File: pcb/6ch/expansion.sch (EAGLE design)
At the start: 48 parts, among them IC3 STM32F042F4, J7 AUDIO_JACK_3.5MM_PTH, J8 AUDIO_JACK_3.5MM_PTH, SW3 324_SW, SW4 324_SW, U1 USBC_16P, U2 USBC_16P, U4 XC6206_DEV

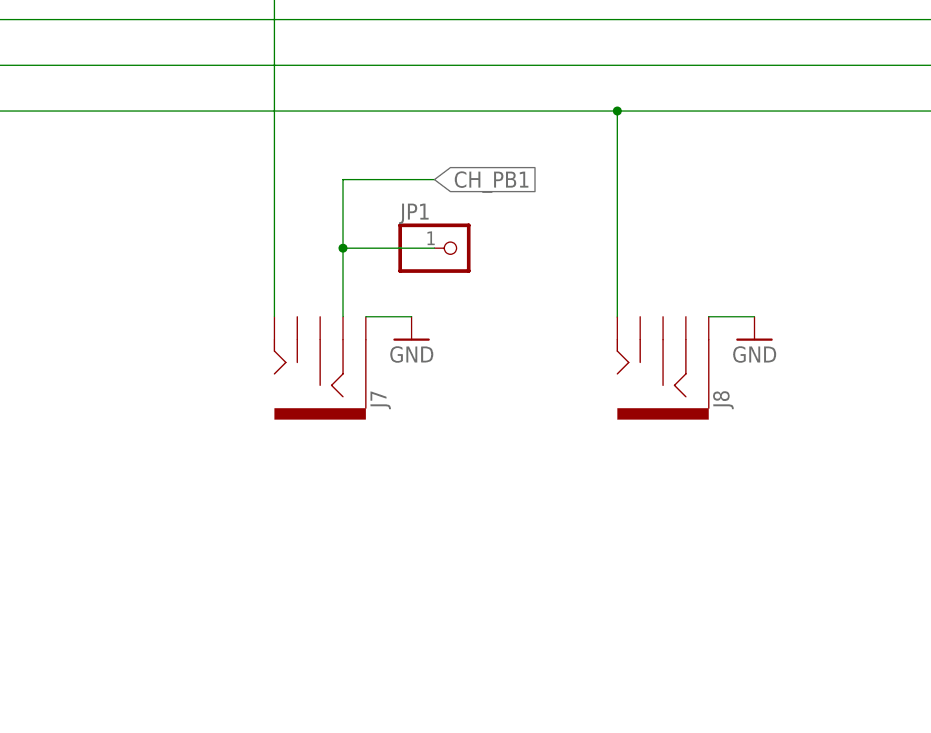
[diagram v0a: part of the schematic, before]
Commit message: added PB1 LED
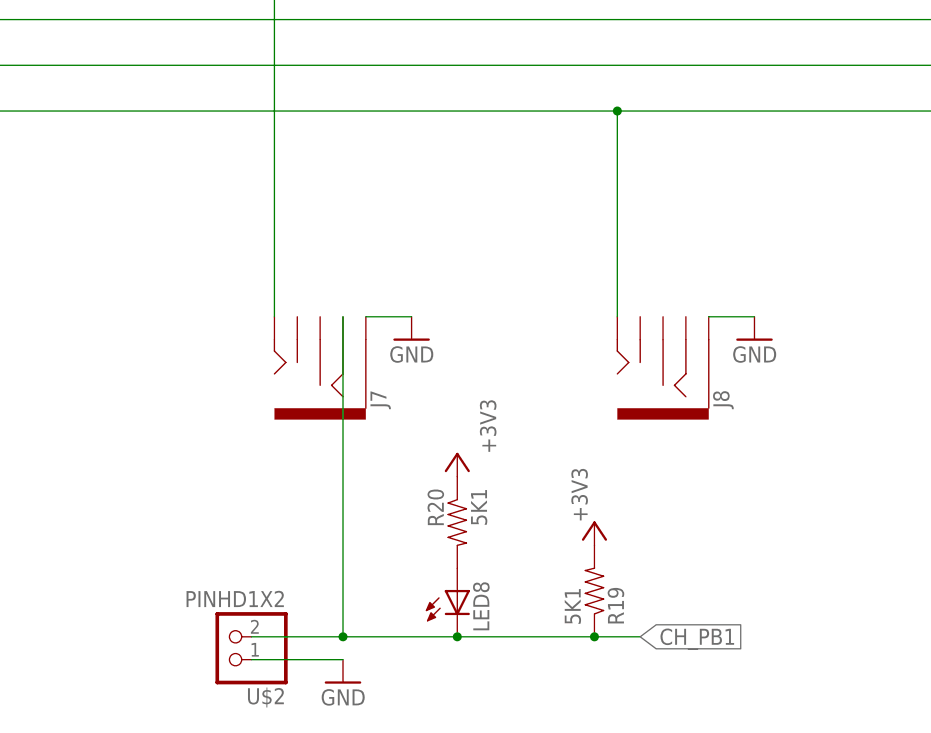
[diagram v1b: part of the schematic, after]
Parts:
- removed JP1: (no value), adafruit_changed:PINHD-1X1CB
- added LED8: (no value), adafruit:LEDCHIP-LED0805
- added R19, R20: 5K1, joyAnalog:RESISTOR0805-RES
- added U$2: PINHD1X2, adafruit_changed:PINHD1X2
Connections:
- new net N$9: LED8.A, R20.2
- net +3V3: now also R19.2, R20.1
- net CH_PB1: now also LED8.C, R19.1, U$2.2; no longer JP1.1
- net GND: now also U$2.1
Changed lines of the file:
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@@
 <part name="GND15" library="supply1" deviceset="GND" device=""/>
 <part name="GND17" library="supply1" deviceset="GND" device=""/>
-<part name="JP1" library="adafruit_changed" deviceset="PINHD-1X1" device="CB"/>
 <part name="JP2" library="pinhead" library_urn="urn:adsk.eagle:library:325" deviceset="PINHD-2X3" device="" package3d_urn="urn:adsk.eagle:package:22462/2"/>
 <part name="GND19" library="supply1" deviceset="GND" device=""/>
@@
 <part name="U$1" library="adafruit_changed" deviceset="PINHD1X2" device=""/>
 <part name="U$3" library="adafruit_changed" deviceset="PINHD1X2" device=""/>
+<part name="R19" library="joyAnalog" deviceset="RESISTOR" device="0805-RES" value="5K1"/>
+<part name="+3V20" library="supply1" library_urn="urn:adsk.eagle:library:371" deviceset="+3V3" device=""/>
+<part name="LED8" library="adafruit" deviceset="LED" device="CHIP-LED0805"/>
+<part name="R20" library="joyAnalog" deviceset="RESISTOR" device="0805-RES" value="5K1"/>
+<part name="+3V21" library="supply1" library_urn="urn:adsk.eagle:library:371" deviceset="+3V3" device=""/>
+<part name="U$2" library="adafruit_changed" deviceset="PINHD1X2" device=""/>
+<part name="GND21" library="supply1" deviceset="GND" device=""/>
 </parts>
 <sheets>
@@
 <attribute name="VALUE" x="-86.36" y="-111.76" size="1.778" layer="96" rot="MR0"/>
 </instance>
-<instance part="JP1" gate="G$1" x="-121.92" y="-99.06" smashed="yes">
-<attribute name="NAME" x="-128.27" y="-95.885" size="1.778" layer="95"/>
-<attribute name="VALUE" x="-128.27" y="-104.14" size="1.778" layer="96"/>
-</instance>
 <instance part="JP2" gate="A" x="149.86" y="-43.18" smashed="yes">
 <attribute name="NAME" x="143.51" y="-37.465" size="1.778" layer="95"/>
@@
 <attribute name="NAME" x="-34.29" y="-27.305" size="1.778" layer="95"/>
 <attribute name="VALUE" x="-34.29" y="-38.1" size="1.778" layer="96"/>
+</instance>
+<instance part="R19" gate="G$1" x="-106.68" y="-137.16" smashed="yes" rot="MR90">
+<attribute name="NAME" x="-105.1814" y="-140.97" size="1.778" layer="95" rot="MR90"/>
+<attribute name="VALUE" x="-109.982" y="-140.97" size="1.778" layer="96" rot="MR90"/>
+<attribute name="NAME" x="-105.1814" y="-140.97" size="1.778" layer="95" rot="MR90"/>
+<attribute name="VALUE" x="-109.982" y="-140.97" size="1.778" layer="96" rot="MR90"/>
+</instance>
+<instance part="+3V20" gate="G$1" x="-106.68" y="-129.54" smashed="yes" rot="MR0">
+<attribute name="VALUE" x="-109.22" y="-129.54" size="1.778" layer="96" rot="MR90"/>
+</instance>
+<instance part="LED8" gate="G$1" x="-121.92" y="-137.16" smashed="yes">
+<attribute name="NAME" x="-118.364" y="-141.732" size="1.778" layer="95" rot="R90"/>
+<attribute name="VALUE" x="-116.205" y="-141.732" size="1.778" layer="96" rot="R90"/>
+</instance>
+<instance part="R20" gate="G$1" x="-121.92" y="-129.54" smashed="yes" rot="MR270">
+<attribute name="NAME" x="-123.4186" y="-125.73" size="1.778" layer="95" rot="MR270"/>
+<attribute name="VALUE" x="-118.618" y="-125.73" size="1.778" layer="96" rot="MR270"/>
+<attribute name="NAME" x="-123.4186" y="-125.73" size="1.778" layer="95" rot="MR270"/>
+<attribute name="VALUE" x="-118.618" y="-125.73" size="1.778" layer="96" rot="MR270"/>
+</instance>
+<instance part="+3V21" gate="G$1" x="-121.92" y="-121.92" smashed="yes" rot="MR0">
+<attribute name="VALUE" x="-119.38" y="-121.92" size="1.778" layer="96" rot="MR90"/>
+</instance>
+<instance part="U$2" gate="1" x="-147.32" y="-142.24" smashed="yes" rot="R180">
+<attribute name="NAME" x="-140.97" y="-147.955" size="1.778" layer="95" rot="R180"/>
+<attribute name="VALUE" x="-140.97" y="-137.16" size="1.778" layer="96" rot="R180"/>
+</instance>
+<instance part="GND21" gate="1" x="-134.62" y="-147.32" smashed="yes" rot="MR0">
+<attribute name="VALUE" x="-132.08" y="-149.86" size="1.778" layer="96" rot="MR0"/>
 </instance>
 </instances>
@@
 <junction x="147.32" y="-43.18"/>
 </segment>
+<segment>
+<pinref part="U$2" gate="1" pin="1"/>
+<pinref part="GND21" gate="1" pin="GND"/>
+<wire x1="-144.78" y1="-144.78" x2="-134.62" y2="-144.78" width="0.1524" layer="91"/>
+</segment>
 </net>
 <net name="+3V3" class="0">
@@
 <wire x1="154.94" y1="-45.72" x2="147.32" y2="-45.72" width="0.1524" layer="91"/>
 <junction x="154.94" y="-45.72"/>
+</segment>
+<segment>
+<pinref part="R19" gate="G$1" pin="2"/>
+<pinref part="+3V20" gate="G$1" pin="+3V3"/>
+</segment>
+<segment>
+<pinref part="R20" gate="G$1" pin="1"/>
+<pinref part="+3V21" gate="G$1" pin="+3V3"/>
 </segment>
 </net>
@@
 </segment>
 <segment>
-<wire x1="-124.46" y1="-91.44" x2="-134.62" y2="-91.44" width="0.1524" layer="91"/>
-<label x="-124.46" y="-91.44" size="1.778" layer="95" xref="yes"/>
+<wire x1="-101.6" y1="-142.24" x2="-106.68" y2="-142.24" width="0.1524" layer="91"/>
+<label x="-101.6" y="-142.24" size="1.778" layer="95" xref="yes"/>
 <pinref part="J7" gate="G$1" pin="RING"/>
-<wire x1="-134.62" y1="-106.68" x2="-134.62" y2="-99.06" width="0.1524" layer="91"/>
-<pinref part="JP1" gate="G$1" pin="1"/>
-<wire x1="-134.62" y1="-99.06" x2="-134.62" y2="-91.44" width="0.1524" layer="91"/>
-<wire x1="-124.46" y1="-99.06" x2="-134.62" y2="-99.06" width="0.1524" layer="91"/>
-<junction x="-134.62" y="-99.06"/>
+<wire x1="-106.68" y1="-142.24" x2="-121.92" y2="-142.24" width="0.1524" layer="91"/>
+<wire x1="-121.92" y1="-142.24" x2="-134.62" y2="-142.24" width="0.1524" layer="91"/>
+<wire x1="-134.62" y1="-106.68" x2="-134.62" y2="-142.24" width="0.1524" layer="91"/>
+<pinref part="R19" gate="G$1" pin="1"/>
+<junction x="-106.68" y="-142.24"/>
+<pinref part="LED8" gate="G$1" pin="C"/>
+<junction x="-121.92" y="-142.24"/>
+<pinref part="U$2" gate="1" pin="2"/>
+<wire x1="-134.62" y1="-142.24" x2="-144.78" y2="-142.24" width="0.1524" layer="91"/>
+<junction x="-134.62" y="-142.24"/>
 </segment>
 </net>
@@
 </segment>
 </net>
+<net name="N$9" class="0">
+<segment>
+<pinref part="LED8" gate="G$1" pin="A"/>
+<pinref part="R20" gate="G$1" pin="2"/>
+</segment>
+</net>

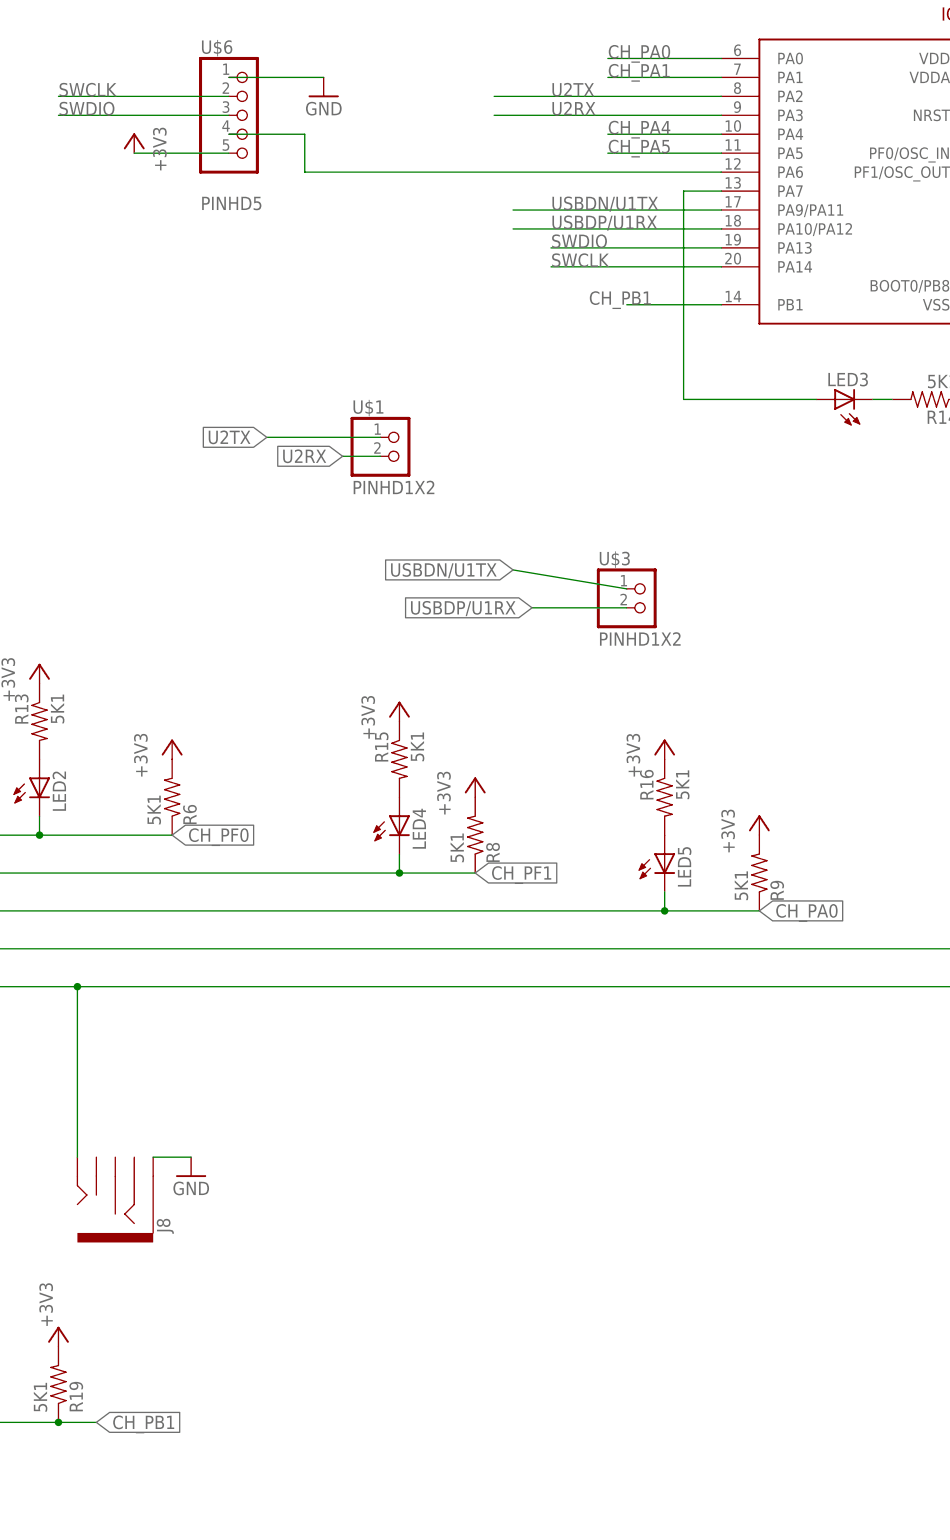
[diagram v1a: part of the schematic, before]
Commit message: added 2 aux channels, cleanup
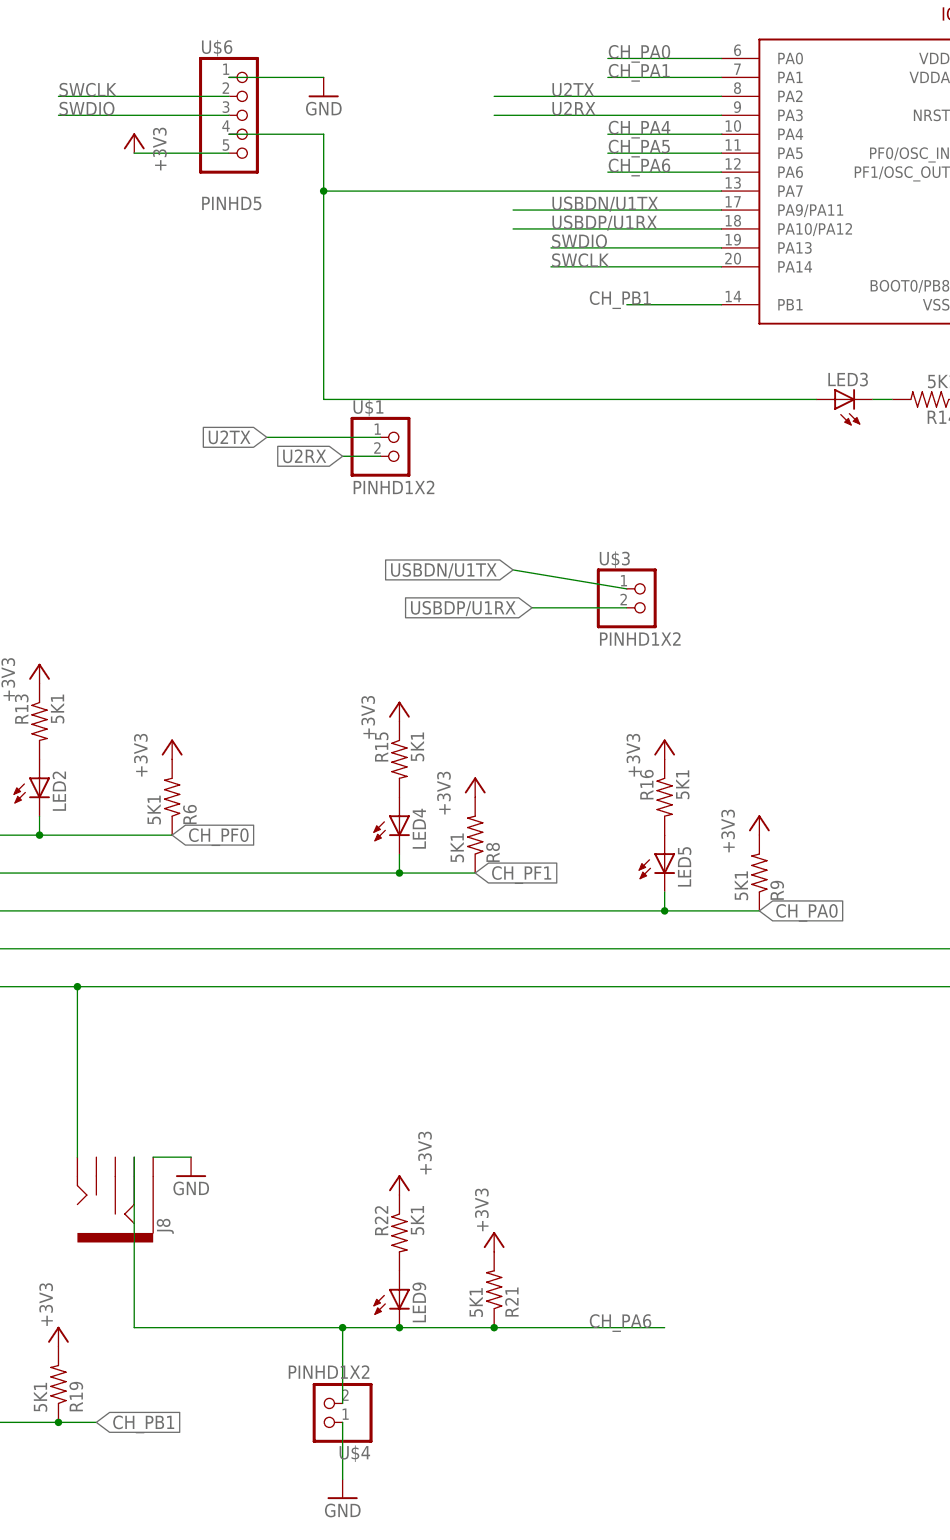
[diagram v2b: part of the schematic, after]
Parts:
- added LED9: (no value), adafruit:LEDCHIP-LED0805
- added R21, R22: 5K1, joyAnalog:RESISTOR0805-RES
- added U$4: PINHD1X2, adafruit_changed:PINHD1X2
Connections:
- removed net N$14: IC3.PA6, U$6.4
- new net CH_PA6: IC3.PA6, J8.RING, LED9.C, R21.1, U$4.2
- new net N$10: IC3.PA7, LED3.A, U$6.4
- net +3V3: now also R21.2, R22.1
- net GND: now also U$4.1
- net N$12: now also LED9.A, R22.2; no longer IC3.PA7, LED3.A
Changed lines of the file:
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@@
 <part name="U$2" library="adafruit_changed" deviceset="PINHD1X2" device=""/>
 <part name="GND21" library="supply1" deviceset="GND" device=""/>
+<part name="R21" library="joyAnalog" deviceset="RESISTOR" device="0805-RES" value="5K1"/>
+<part name="+3V22" library="supply1" library_urn="urn:adsk.eagle:library:371" deviceset="+3V3" device=""/>
+<part name="LED9" library="adafruit" deviceset="LED" device="CHIP-LED0805"/>
+<part name="R22" library="joyAnalog" deviceset="RESISTOR" device="0805-RES" value="5K1"/>
+<part name="+3V23" library="supply1" library_urn="urn:adsk.eagle:library:371" deviceset="+3V3" device=""/>
+<part name="U$4" library="adafruit_changed" deviceset="PINHD1X2" device=""/>
+<part name="GND22" library="supply1" deviceset="GND" device=""/>
 </parts>
 <sheets>
@@
 <instance part="GND21" gate="1" x="-134.62" y="-147.32" smashed="yes" rot="MR0">
 <attribute name="VALUE" x="-132.08" y="-149.86" size="1.778" layer="96" rot="MR0"/>
+</instance>
+<instance part="R21" gate="G$1" x="-48.26" y="-124.46" smashed="yes" rot="MR90">
+<attribute name="NAME" x="-46.7614" y="-128.27" size="1.778" layer="95" rot="MR90"/>
+<attribute name="VALUE" x="-51.562" y="-128.27" size="1.778" layer="96" rot="MR90"/>
+<attribute name="NAME" x="-46.7614" y="-128.27" size="1.778" layer="95" rot="MR90"/>
+<attribute name="VALUE" x="-51.562" y="-128.27" size="1.778" layer="96" rot="MR90"/>
+</instance>
+<instance part="+3V22" gate="G$1" x="-48.26" y="-116.84" smashed="yes" rot="MR0">
+<attribute name="VALUE" x="-50.8" y="-116.84" size="1.778" layer="96" rot="MR90"/>
+</instance>
+<instance part="LED9" gate="G$1" x="-60.96" y="-124.46" smashed="yes">
+<attribute name="NAME" x="-57.404" y="-129.032" size="1.778" layer="95" rot="R90"/>
+<attribute name="VALUE" x="-55.245" y="-129.032" size="1.778" layer="96" rot="R90"/>
+</instance>
+<instance part="R22" gate="G$1" x="-60.96" y="-116.84" smashed="yes" rot="MR270">
+<attribute name="NAME" x="-62.4586" y="-113.03" size="1.778" layer="95" rot="MR270"/>
+<attribute name="VALUE" x="-57.658" y="-113.03" size="1.778" layer="96" rot="MR270"/>
+<attribute name="NAME" x="-62.4586" y="-113.03" size="1.778" layer="95" rot="MR270"/>
+<attribute name="VALUE" x="-57.658" y="-113.03" size="1.778" layer="96" rot="MR270"/>
+</instance>
+<instance part="+3V23" gate="G$1" x="-60.96" y="-109.22" smashed="yes" rot="MR0">
+<attribute name="VALUE" x="-58.42" y="-109.22" size="1.778" layer="96" rot="MR90"/>
+</instance>
+<instance part="U$4" gate="1" x="-71.12" y="-139.7" smashed="yes" rot="R180">
+<attribute name="NAME" x="-64.77" y="-145.415" size="1.778" layer="95" rot="R180"/>
+<attribute name="VALUE" x="-64.77" y="-134.62" size="1.778" layer="96" rot="R180"/>
+</instance>
+<instance part="GND22" gate="1" x="-68.58" y="-152.4" smashed="yes" rot="MR0">
+<attribute name="VALUE" x="-66.04" y="-154.94" size="1.778" layer="96" rot="MR0"/>
 </instance>
 </instances>
@@
 <wire x1="-144.78" y1="-144.78" x2="-134.62" y2="-144.78" width="0.1524" layer="91"/>
 </segment>
+<segment>
+<pinref part="U$4" gate="1" pin="1"/>
+<pinref part="GND22" gate="1" pin="GND"/>
+<wire x1="-68.58" y1="-142.24" x2="-68.58" y2="-149.86" width="0.1524" layer="91"/>
+</segment>
 </net>
 <net name="+3V3" class="0">
@@
 <pinref part="R20" gate="G$1" pin="1"/>
 <pinref part="+3V21" gate="G$1" pin="+3V3"/>
+</segment>
+<segment>
+<pinref part="R21" gate="G$1" pin="2"/>
+<pinref part="+3V22" gate="G$1" pin="+3V3"/>
+</segment>
+<segment>
+<pinref part="R22" gate="G$1" pin="1"/>
+<pinref part="+3V23" gate="G$1" pin="+3V3"/>
 </segment>
 </net>
@@
 <pinref part="R14" gate="G$1" pin="2"/>
 <wire x1="5.08" y1="-5.08" x2="2.54" y2="-5.08" width="0.1524" layer="91"/>
-</segment>
-</net>
-<net name="N$12" class="0">
-<segment>
-<pinref part="IC3" gate="G$1" pin="PA7"/>
-<pinref part="LED3" gate="G$1" pin="A"/>
-<wire x1="-17.78" y1="22.86" x2="-22.86" y2="22.86" width="0.1524" layer="91"/>
-<wire x1="-22.86" y1="22.86" x2="-22.86" y2="-5.08" width="0.1524" layer="91"/>
-<wire x1="-22.86" y1="-5.08" x2="-5.08" y2="-5.08" width="0.1524" layer="91"/>
-</segment>
-</net>
-<net name="N$14" class="0">
-<segment>
-<pinref part="IC3" gate="G$1" pin="PA6"/>
-<wire x1="-17.78" y1="25.4" x2="-73.66" y2="25.4" width="0.1524" layer="91"/>
-<pinref part="U$6" gate="G$1" pin="4"/>
-<wire x1="-73.66" y1="25.4" x2="-73.66" y2="30.48" width="0.1524" layer="91"/>
-<wire x1="-73.66" y1="30.48" x2="-83.82" y2="30.48" width="0.1524" layer="91"/>
 </segment>
 </net>
@@
 </segment>
 </net>
+<net name="N$10" class="0">
+<segment>
+<pinref part="IC3" gate="G$1" pin="PA7"/>
+<wire x1="-17.78" y1="22.86" x2="-71.12" y2="22.86" width="0.1524" layer="91"/>
+<wire x1="-71.12" y1="22.86" x2="-71.12" y2="30.48" width="0.1524" layer="91"/>
+<pinref part="U$6" gate="G$1" pin="4"/>
+<wire x1="-71.12" y1="30.48" x2="-83.82" y2="30.48" width="0.1524" layer="91"/>
+<pinref part="LED3" gate="G$1" pin="A"/>
+<wire x1="-71.12" y1="22.86" x2="-71.12" y2="-5.08" width="0.1524" layer="91"/>
+<wire x1="-71.12" y1="-5.08" x2="-5.08" y2="-5.08" width="0.1524" layer="91"/>
+<junction x="-71.12" y="22.86"/>
+</segment>
+</net>
+<net name="CH_PA6" class="0">
+<segment>
+<pinref part="IC3" gate="G$1" pin="PA6"/>
+<wire x1="-17.78" y1="25.4" x2="-33.02" y2="25.4" width="0.1524" layer="91"/>
+<label x="-33.02" y="25.4" size="1.778" layer="95"/>
+</segment>
+<segment>
+<pinref part="J8" gate="G$1" pin="RING"/>
+<wire x1="-96.52" y1="-106.68" x2="-96.52" y2="-129.54" width="0.1524" layer="91"/>
+<label x="-35.56" y="-129.54" size="1.778" layer="95"/>
+<wire x1="-96.52" y1="-129.54" x2="-68.58" y2="-129.54" width="0.1524" layer="91"/>
+<pinref part="R21" gate="G$1" pin="1"/>
+<wire x1="-68.58" y1="-129.54" x2="-60.96" y2="-129.54" width="0.1524" layer="91"/>
+<wire x1="-60.96" y1="-129.54" x2="-48.26" y2="-129.54" width="0.1524" layer="91"/>
+<wire x1="-48.26" y1="-129.54" x2="-25.4" y2="-129.54" width="0.1524" layer="91"/>
+<junction x="-48.26" y="-129.54"/>
+<pinref part="LED9" gate="G$1" pin="C"/>
+<junction x="-60.96" y="-129.54"/>
+<pinref part="U$4" gate="1" pin="2"/>
+<wire x1="-68.58" y1="-129.54" x2="-68.58" y2="-139.7" width="0.1524" layer="91"/>
+<junction x="-68.58" y="-129.54"/>
+</segment>
+</net>
+<net name="N$12" class="0">
+<segment>
+<pinref part="LED9" gate="G$1" pin="A"/>
+<pinref part="R22" gate="G$1" pin="2"/>
+</segment>
+</net>
